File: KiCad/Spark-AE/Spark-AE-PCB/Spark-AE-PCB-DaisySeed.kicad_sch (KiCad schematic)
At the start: 3 parts, among them J1 Conn_01x20_Pin, J2 Conn_01x20_Pin, U1 Daisy_Seed

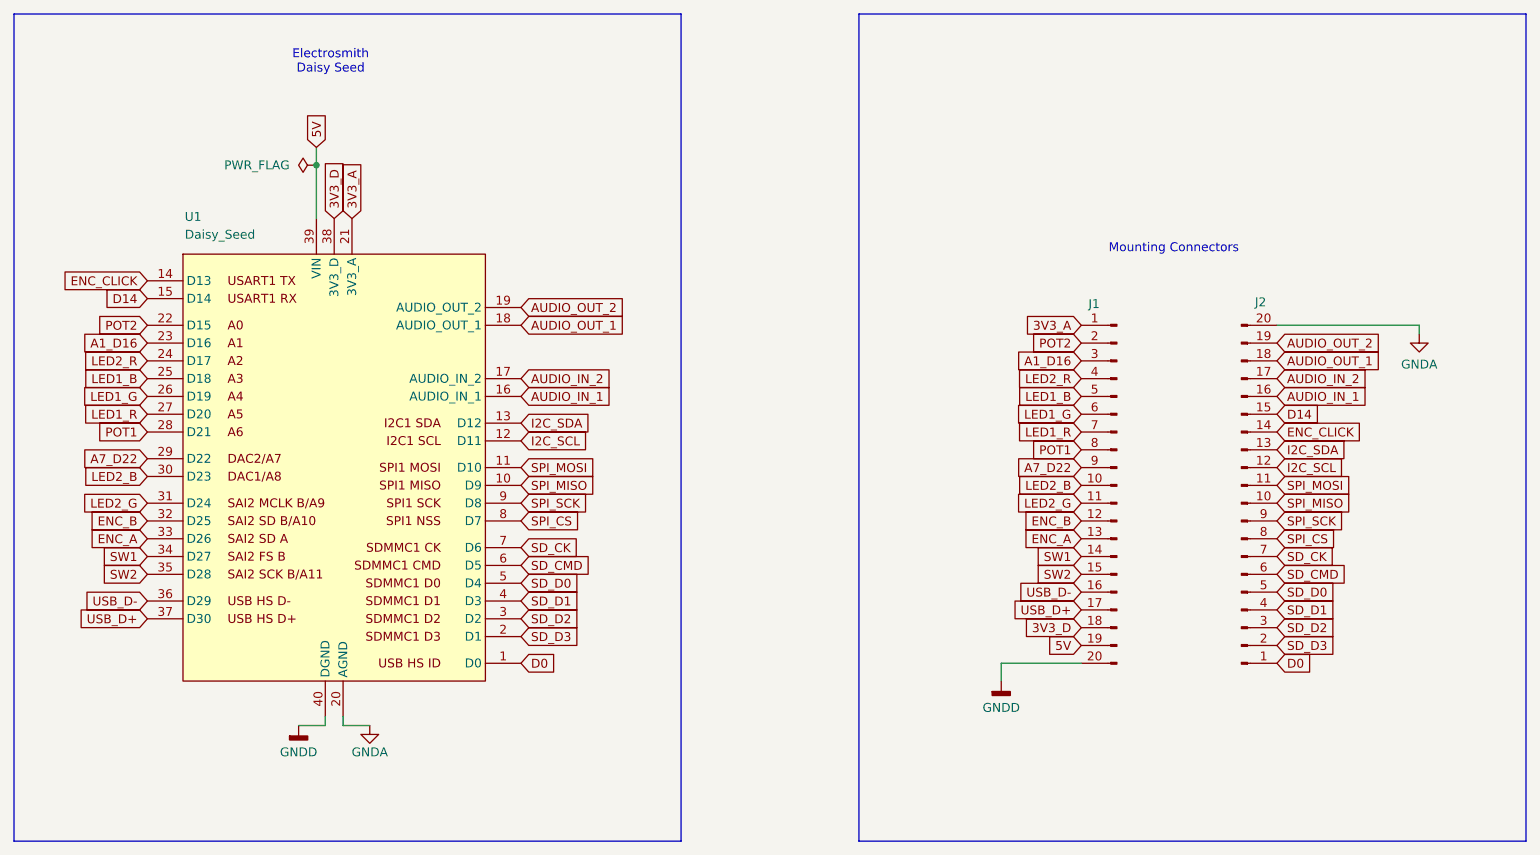
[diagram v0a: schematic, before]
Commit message: assigned footprints & sorted ratsnest
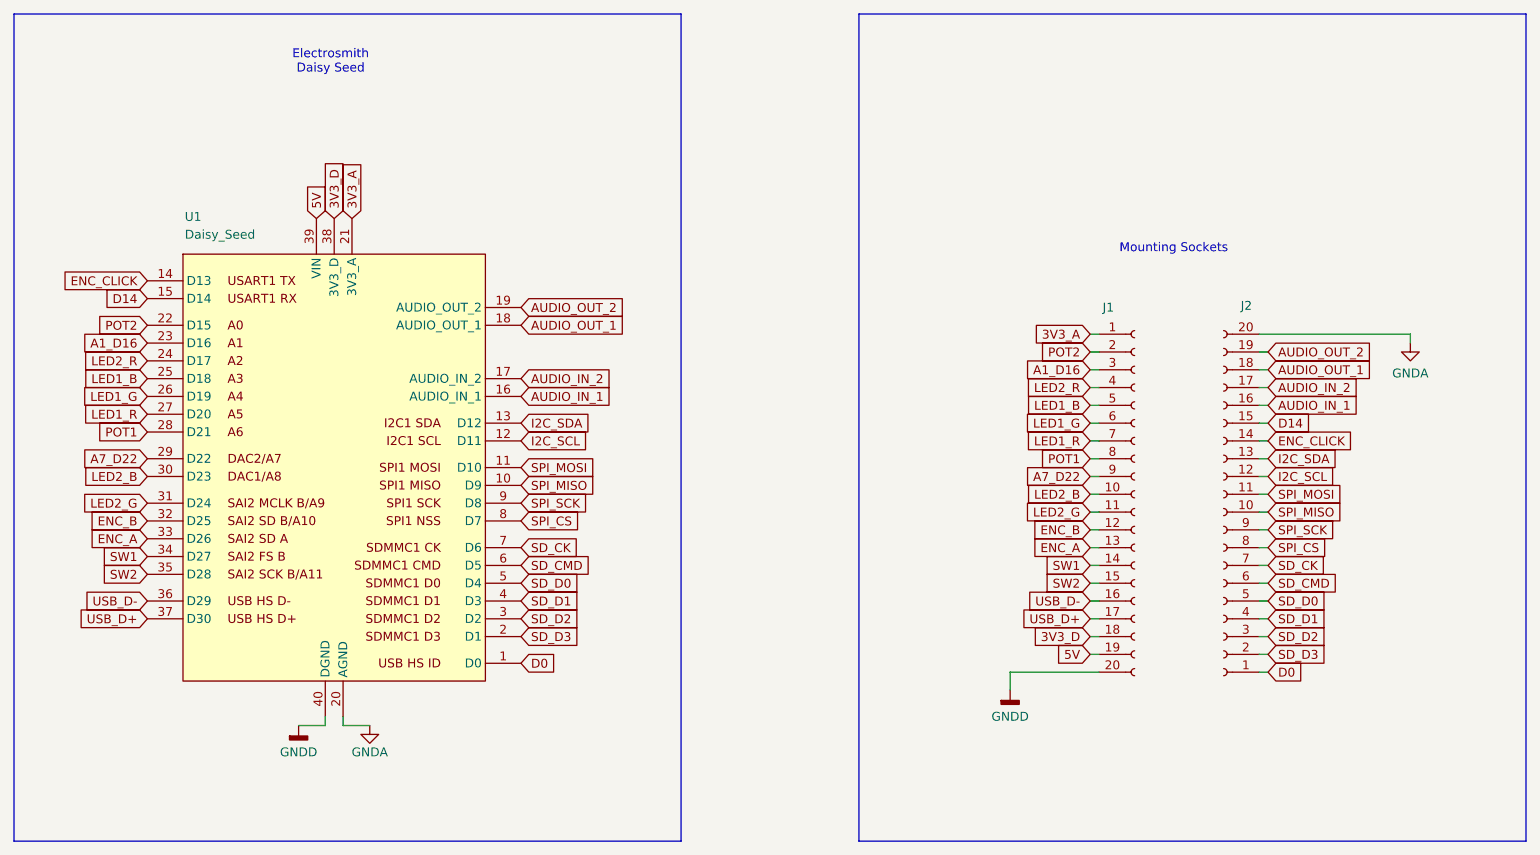
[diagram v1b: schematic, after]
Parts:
- removed J1, J2: Conn_01x20_Pin, symbol Connector:Conn_01x20_Pin
- added J1, J2: Conn_01x20_Socket, clectric-diy:Connector_PinSocket-1x20-P2.54mm-H1.27mm_Mill-Max_315-13-120-41-004000, symbol Connector:Conn_01x20_Socket
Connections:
- net 3V3_A: now also J1.1 (Pin_1)
- net 3V3_D: now also J1.18 (Pin_18)
- net 5V: now also J1.19 (Pin_19)
- net A1_D16: now also J1.3 (Pin_3)
- net A7_D22: now also J1.9 (Pin_9)
- net AUDIO_IN_1: now also J2.16 (Pin_16)
- net AUDIO_IN_2: now also J2.17 (Pin_17)
- net AUDIO_OUT_1: now also J2.18 (Pin_18)
- net AUDIO_OUT_2: now also J2.19 (Pin_19)
- net D0: now also J2.1 (Pin_1)
- net D14: now also J2.15 (Pin_15)
- net ENC_A: now also J1.13 (Pin_13)
- net ENC_B: now also J1.12 (Pin_12)
- net ENC_CLICK: now also J2.14 (Pin_14)
- net GNDA: now also J2.20 (Pin_20)
- net GNDD: now also J1.20 (Pin_20)
- net I2C_SCL: now also J2.12 (Pin_12)
- net I2C_SDA: now also J2.13 (Pin_13)
- net LED1_B: now also J1.5 (Pin_5)
- net LED1_G: now also J1.6 (Pin_6)
- net LED1_R: now also J1.7 (Pin_7)
- net LED2_B: now also J1.10 (Pin_10)
- net LED2_G: now also J1.11 (Pin_11)
- net LED2_R: now also J1.4 (Pin_4)
- net POT1: now also J1.8 (Pin_8)
- net POT2: now also J1.2 (Pin_2)
- net SD_CK: now also J2.7 (Pin_7)
- net SD_CMD: now also J2.6 (Pin_6)
- net SD_D0: now also J2.5 (Pin_5)
- net SD_D1: now also J2.4 (Pin_4)
- net SD_D2: now also J2.3 (Pin_3)
- net SD_D3: now also J2.2 (Pin_2)
- net SPI_CS: now also J2.8 (Pin_8)
- net SPI_MISO: now also J2.10 (Pin_10)
- net SPI_MOSI: now also J2.11 (Pin_11)
- net SPI_SCK: now also J2.9 (Pin_9)
- net SW1: now also J1.14 (Pin_14)
- net SW2: now also J1.15 (Pin_15)
- net USB_D+: now also J1.17 (Pin_17)
- net USB_D-: now also J1.16 (Pin_16)
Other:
- note added: "Mounting Sockets"
- note removed: "Mounting Connectors"

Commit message: schematic 100% complete. pcb layout around 50% complete.
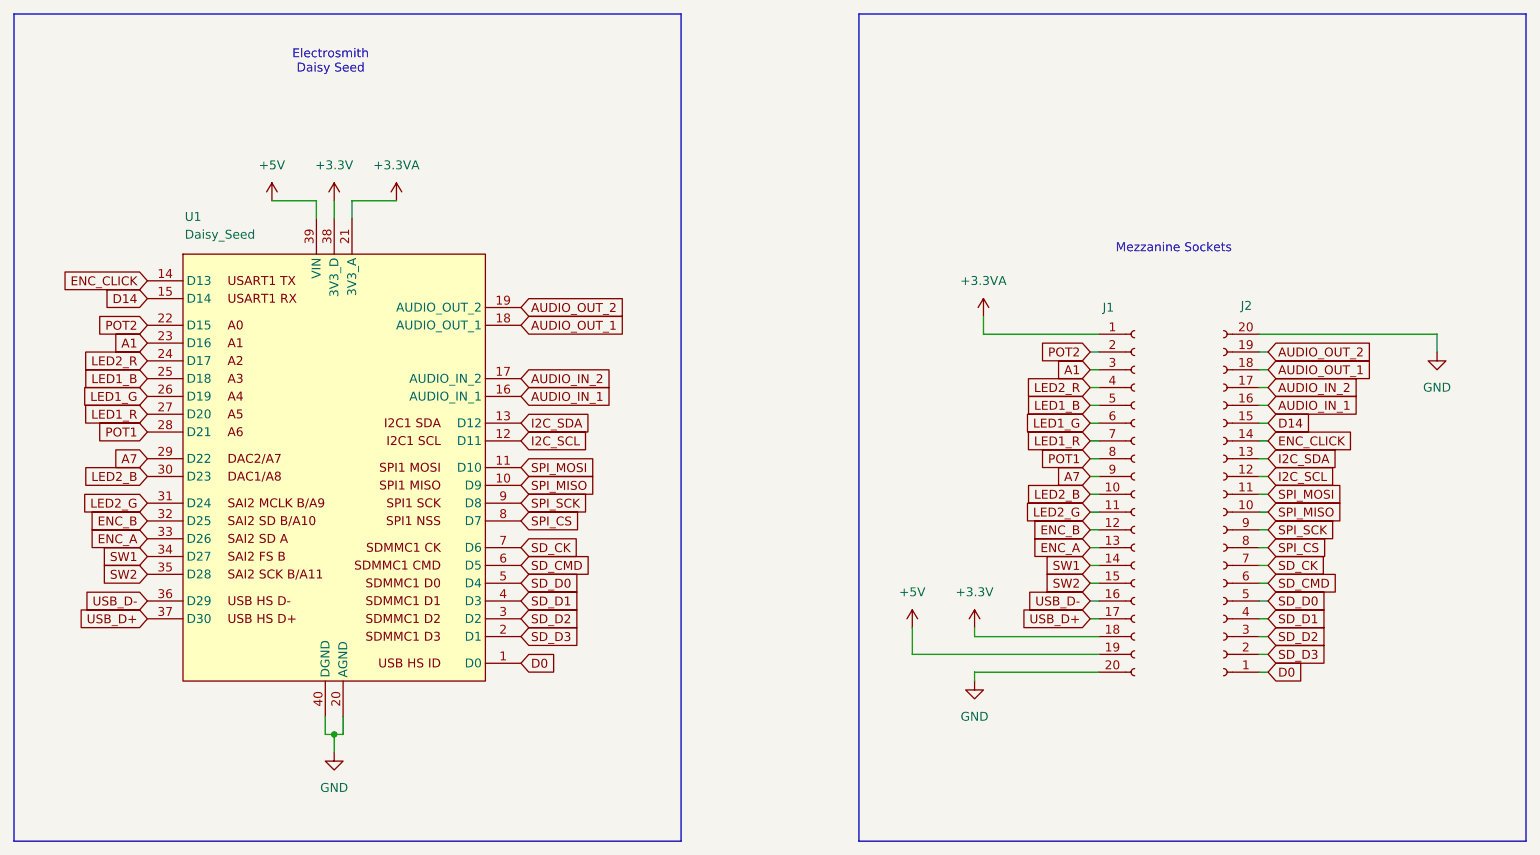
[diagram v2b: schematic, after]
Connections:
- net GNDD is gone; now on net GND: J1.20 (Pin_20), U1.40 (DGND)
- net 3V3_A renamed +3.3VA
- net 3V3_D renamed +3.3V
- net 5V renamed +5V
- net A1_D16 renamed A1
- net A7_D22 renamed A7
- net GNDA renamed GND
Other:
- note added: "Mezzanine Sockets"
- note removed: "Mounting Sockets"

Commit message: pcb layout complete. ready for final pre-fab confirmation.
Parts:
- U1: now left out of the parts list
